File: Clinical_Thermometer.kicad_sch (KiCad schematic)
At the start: 32 parts, among them J1 BM02B-SRSS-TB_LF__SN_, U1 ESP32-C3-MINI-1-N4, U2 AMS1117-3.3, U3 TP4056-42-ESOP8, U4 ER_OLEDM0.91_1x-I2C, U5 DS18B20

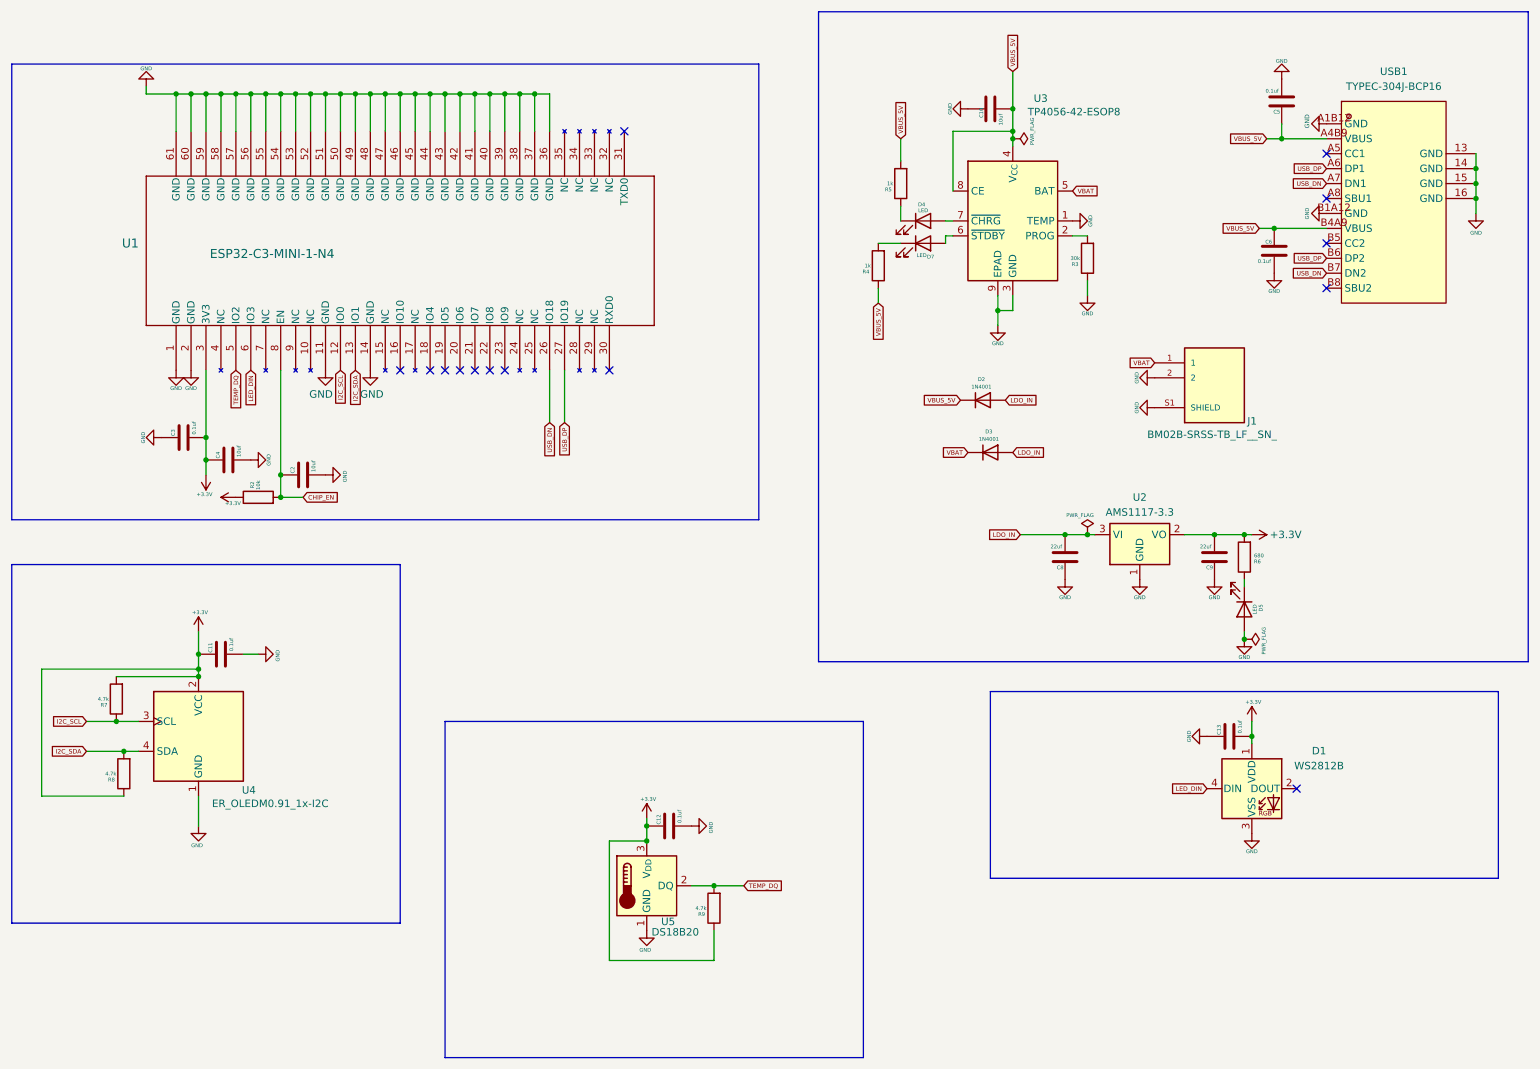
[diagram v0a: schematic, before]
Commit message: Fix gitignore and updated Schematics and PCB Designs
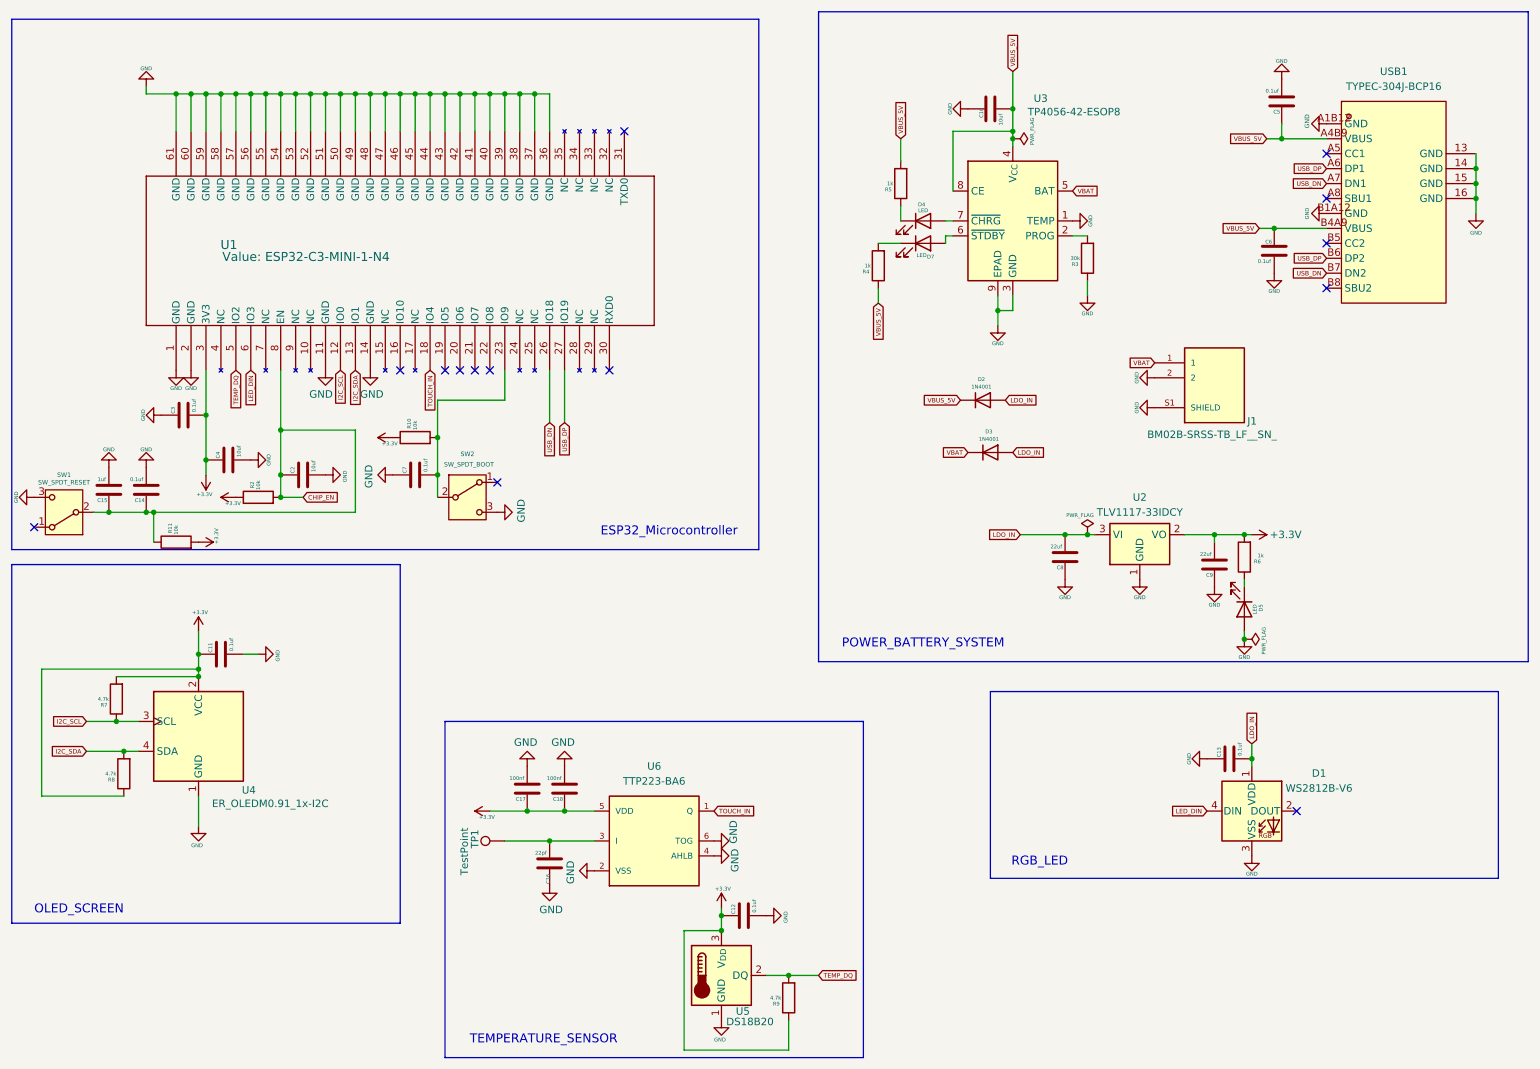
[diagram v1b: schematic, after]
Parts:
- added C14, C7: 0.1uf, Capacitor_SMD:C_0402_1005Metric, symbol Device:C
- added C15: 1uf, Capacitor_SMD:C_0402_1005Metric, symbol Device:C
- added C16: 22pf, Capacitor_SMD:C_0402_1005Metric, symbol Device:C
- added C17, C18: 100nf, Capacitor_SMD:C_0402_1005Metric, symbol Device:C
- added R10, R11: 10k, Resistor_SMD:R_0402_1005Metric, symbol Device:R
- added SW1: SW_SPDT_RESET, Library:PTS636SM25FSMTRLFS, symbol Switch:SW_SPDT
- added SW2: SW_SPDT_BOOT, Library:PTS636SM25FSMTRLFS, symbol Switch:SW_SPDT
- added TP1: TestPoint, TestPoint:TestPoint_Pad_1.0x1.0mm, symbol Connector:TestPoint
- added U6: TTP223-BA6, Package_TO_SOT_SMD:SOT-23-6, symbol TTP223-BA6:TTP223-BA6
- C10, C2, C4: footprint (none) -> Capacitor_SMD:C_0402_1005Metric; LCSC Part (none) -> C315248
- C11, C12, C13, C3, C5, C6: footprint (none) -> Capacitor_SMD:C_0402_1005Metric; LCSC Part (none) -> C131394
- C8, C9: footprint (none) -> Capacitor_SMD:C_0402_1005Metric; LCSC Part (none) -> C3854737
- D1: value WS2812B -> WS2812B-V6; LCSC Part (none) -> C52917433
- D2, D3: footprint Diode_THT:D_DO-41_SOD81_P10.16mm_Horizontal -> Diode_SMD:D_0402_1005Metric; LCSC Part (none) -> C145305
- D4, D5, D7: footprint (none) -> LED_SMD:LED_0402_1005Metric; LCSC Part (none) -> C74338
- J1: LCSC Part (none) -> C160388
- R2: footprint (none) -> Resistor_SMD:R_0402_1005Metric; LCSC Part (none) -> C60490
- R3: footprint (none) -> Resistor_SMD:R_0402_1005Metric; LCSC Part (none) -> C138008
- R4, R5: footprint (none) -> Resistor_SMD:R_0402_1005Metric; LCSC Part (none) -> C106235
- R6: value 680 -> 1k; footprint (none) -> Resistor_SMD:R_0402_1005Metric; LCSC Part (none) -> C106235
- R7, R8, R9: footprint (none) -> Resistor_SMD:R_0402_1005Metric; LCSC Part (none) -> C105871
- U1: footprint ESP32-C3-MINI-1_EXP -> ESP32C3MINII:ESP32-C3-MINI-1_EXP; LCSC Part (none) -> C2838502
- U2: value AMS1117-3.3 -> TLV1117-33IDCY; LCSC Part (none) -> C2877971
- U3: LCSC Part (none) -> C16581
- U4: LCSC Part (none) -> C5248081
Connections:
- net +3.3V: now also C17.1, C18.1, R10.1, R11.2, U6.5 (VDD); no longer C13.2, D1.1 (VDD)
- net CHIP_EN: now also C14.1, C15.1, R11.1, SW1.2 (B)
- net GND: now also C14.2, C15.2, C16.1, C17.2, C18.2, C7.1, SW1.3 (C), SW2.3 (C), U6.2 (VSS), U6.4 (AHLB), U6.6 (TOG)
- net LDO_IN: now also C13.2, D1.1 (VDD)
- net TOUCH_IN: now reaches U1.18 (IO4)
- net TOUCH_IN: now also U6.1 (Q)
- net at U1.23 (IO9): now also C7.2, R10.2, SW2.2 (B)
- new net: C16.2, TP1.1, U6.3 (I)
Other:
- note added: "ESP32_Microcontroller"
- note added: "OLED_SCREEN"
- note added: "POWER_BATTERY_SYSTEM"
- note added: "RGB_LED"
- note added: "TEMPERATURE_SENSOR"
- moved on the sheet: C12, C13, C3, C9, D1, R9, U5
